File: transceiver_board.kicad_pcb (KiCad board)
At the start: 2 copper layers, 212.5 x 77.2 mm, 128 parts, among them J1 85505-5113, J2 Conn_01x01_Male, J3 Laser, J4 Conn_01x01_Male, J5 Receiver Connector, Q1 BC547, Q2 BC547, T1 S558-5999-46-F, U1 LAN83C185-JT, U2 ltc6752ims8-2-pbf, U4 AP63203WU, U5 AP63205WU, U6 LM317_TO-220, U7 LM317_TO-220, Y1 25 MHz

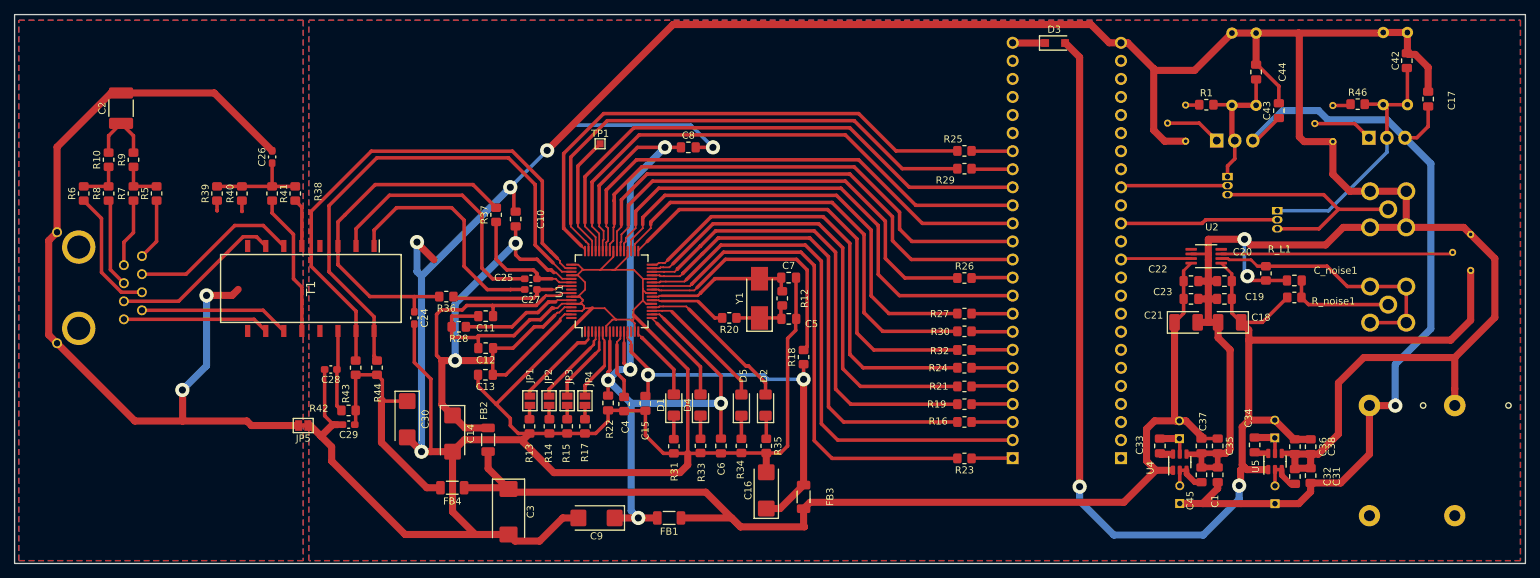
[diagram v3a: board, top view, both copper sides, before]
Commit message: Added revision 0 to copper and moved a via
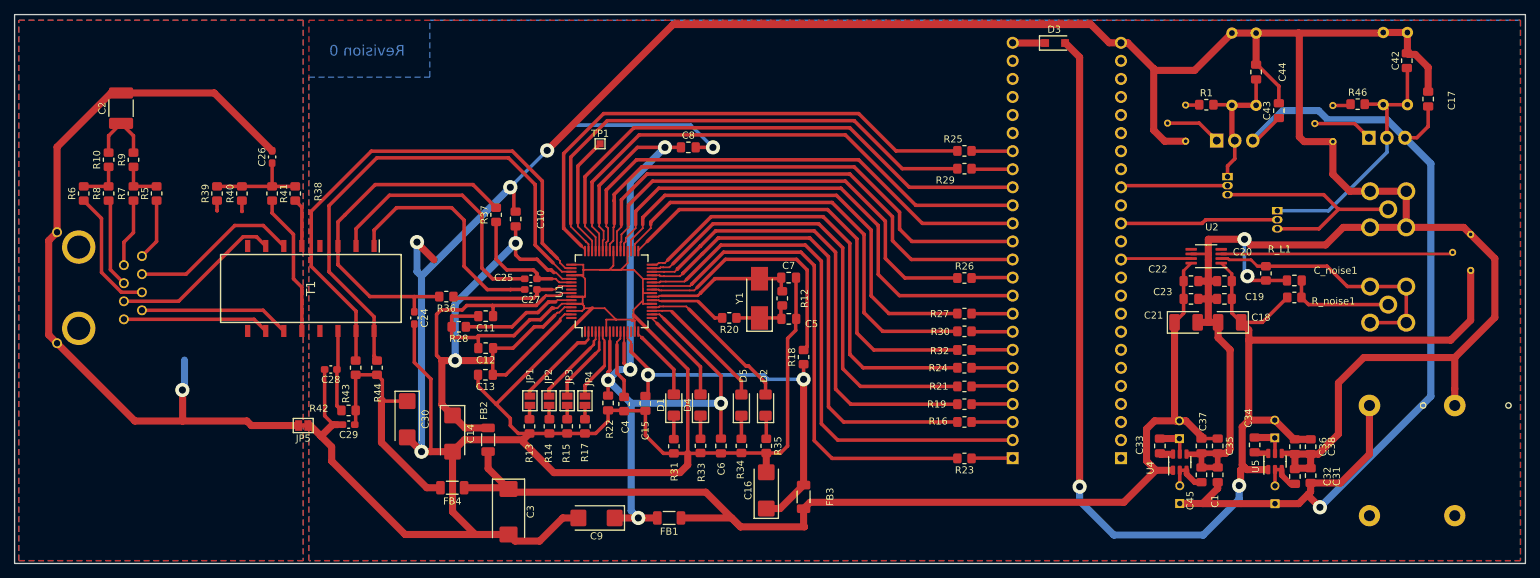
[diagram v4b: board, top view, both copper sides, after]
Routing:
- net +12V: track 122.4 -> 139.9 mm
- net GND1: track 128.0 -> 112.8 mm, vias 2 -> 1
- net GND: track 815.7 -> 820.6 mm
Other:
- board text added: "Revision 0"

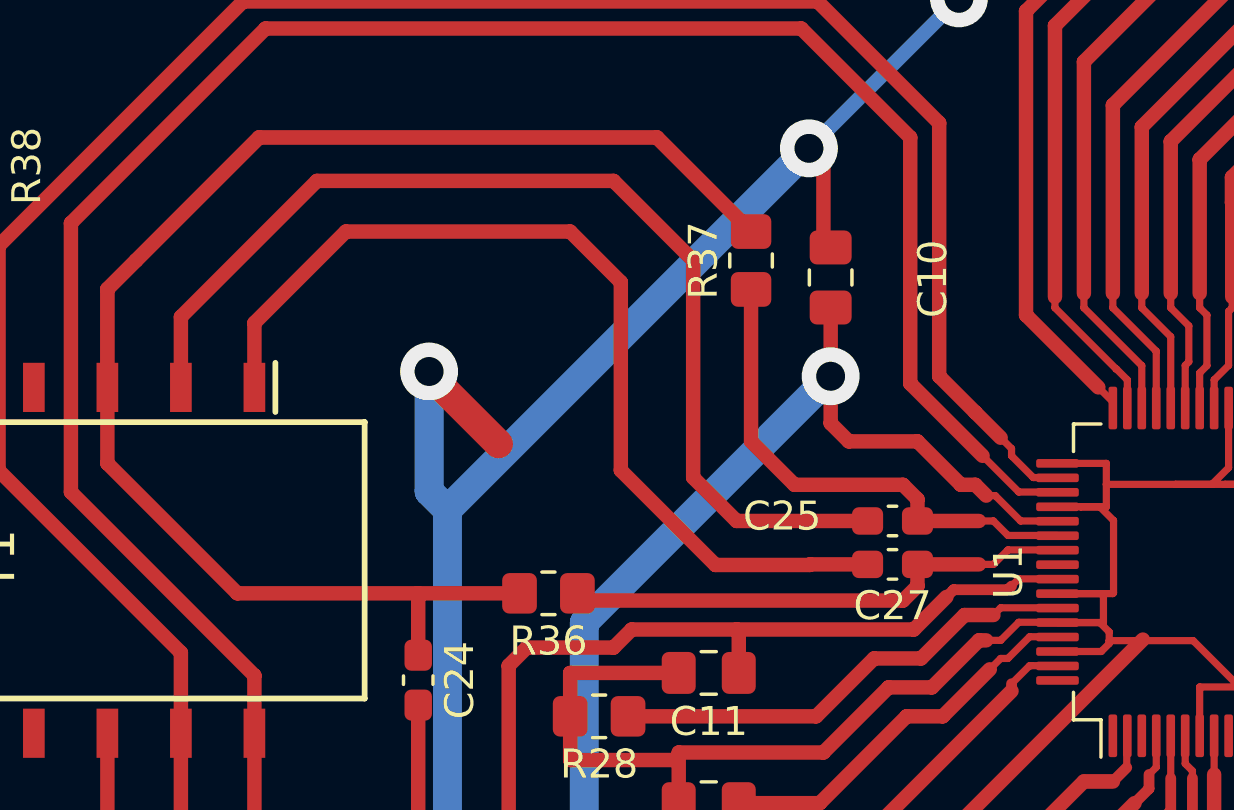
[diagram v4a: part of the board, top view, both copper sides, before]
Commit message: Emergency fixes
Change 6u8 cap foot print and add back copper plane
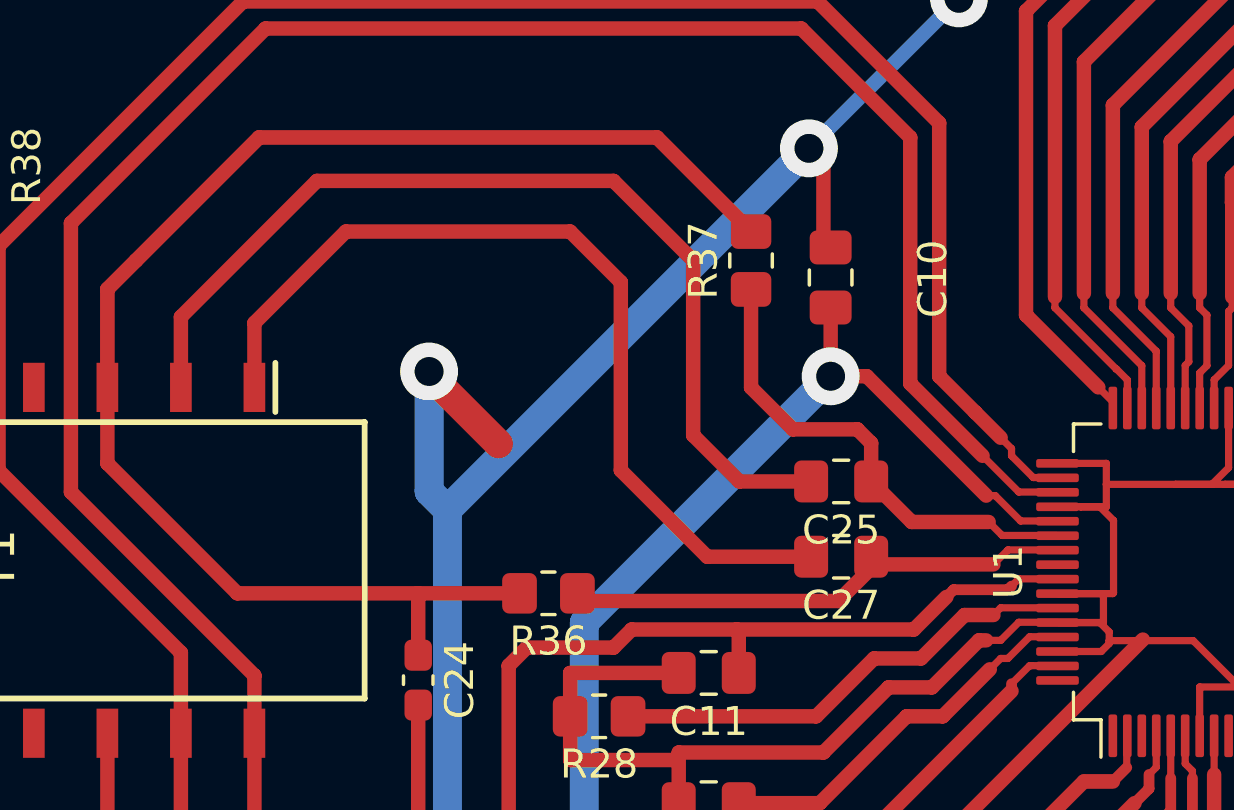
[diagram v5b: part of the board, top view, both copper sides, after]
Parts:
- C25, C27: footprint Capacitor_SMD:C_0603_1608Metric_Pad1.08x0.95mm_HandSolder -> Capacitor_SMD:C_0805_2012Metric_Pad1.18x1.45mm_HandSolder
- moved C25 2.24 mm to (87.2, 77.0)
- moved C27 1.79 mm to (87.2, 79.6)
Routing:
- net Net-(C25-Pad2): track 37.4 -> 34.0 mm
- net Net-(C27-Pad2): track 33.3 -> 31.2 mm
- net PHY-AVDD: track 115.2 -> 114.2 mm
- net MAG-RXN: track 17.6 -> 16.9 mm

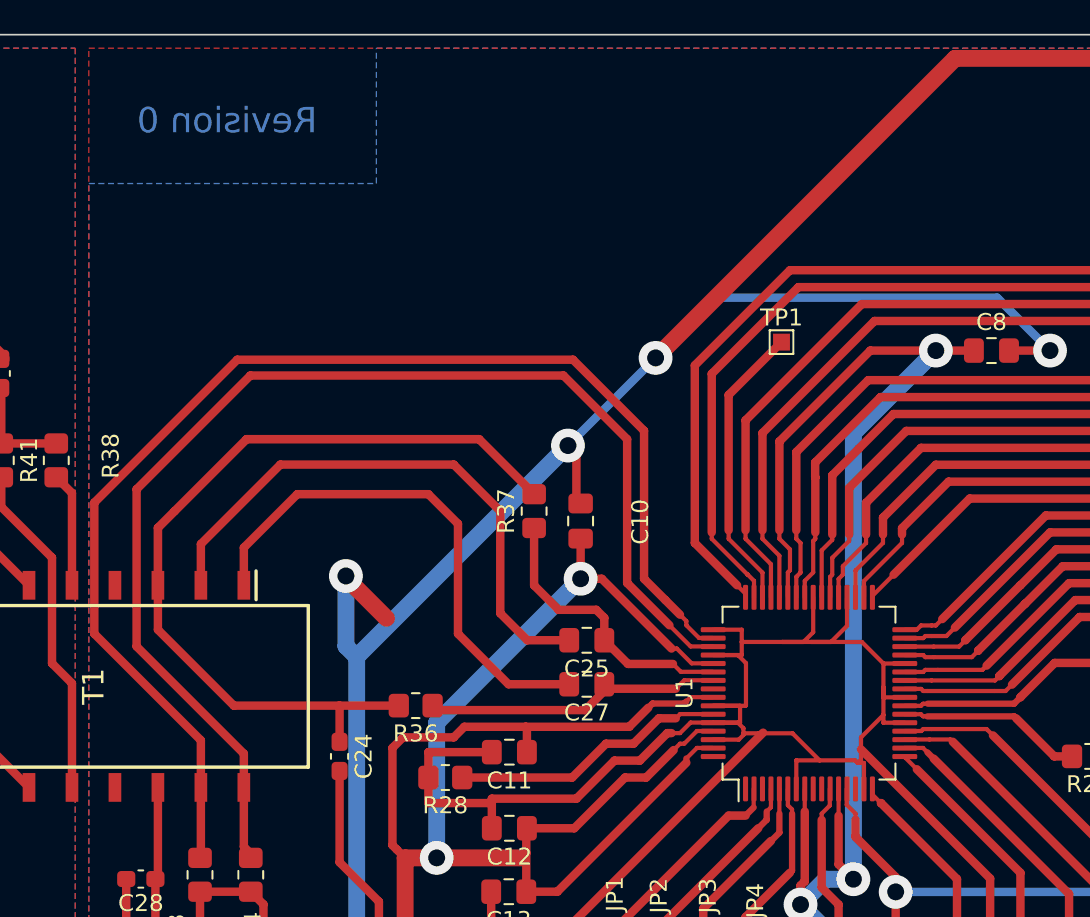
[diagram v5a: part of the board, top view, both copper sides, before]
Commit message: Change QFP footprint to 0.25mm gap
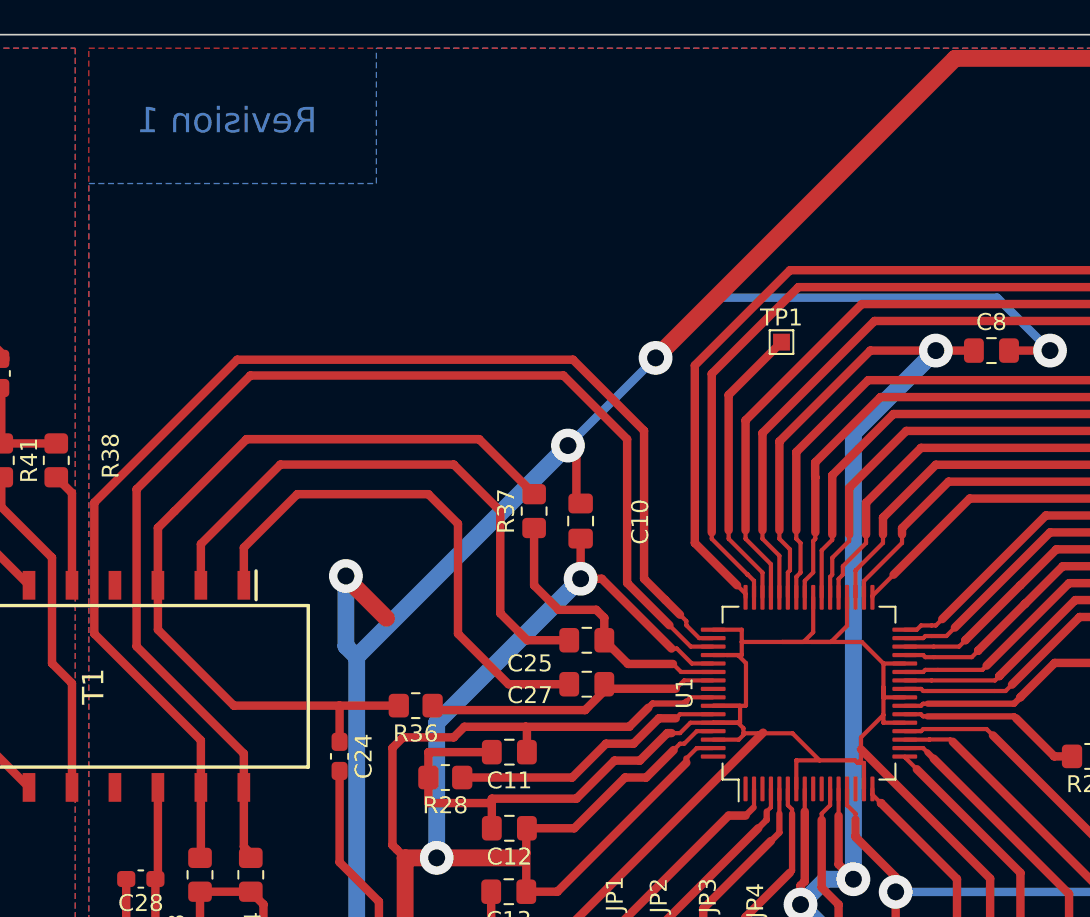
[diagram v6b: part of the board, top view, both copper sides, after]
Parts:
- U1: footprint Package_QFP:TQFP-64_10x10mm_P0.5mm -> FPGA:TQFP-64_10x10mm_P0.5mm
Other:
- board text added: "Revision 1"
- board text removed: "Revision 0"
